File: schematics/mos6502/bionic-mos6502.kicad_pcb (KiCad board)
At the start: 2 copper layers, 25.4 x 68.6 mm, 8 parts, among them J1 Bionic-P135, J2 Bionic-P245, U1 W65C816S, U2 11AA010-I/TT

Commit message: [MOS6502] Cleanup schematics
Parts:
- D1: footprint 0-LocalLibrary:LED_CSL1901UW1_ROM-M -> rhom:LED_CSL1901UW1_ROM-M
- J1: footprint 0-LocalLibrary:Bionic-P135_Vertical -> bionic:Bionic-P135_Vertical
- J2: footprint 0-LocalLibrary:Bionic-P245_Vertical -> bionic:Bionic-P245_Vertical
- U1: footprint 0-LocalLibrary:DIP-40_W15.24mm_Socket -> bionic:DIP-40_W15.24mm_Socket
- U2: footprint 0-LocalLibrary:SOT-23_MC_MCH-M -> microchip:SOT-23_MC_MCH-M
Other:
- rule pad_to_mask_clearance: 0.051 -> 0
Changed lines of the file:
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@@
 	)
 	(setup
-		(pad_to_mask_clearance 0.051)
-		(solder_mask_min_width 0.25)
+		(pad_to_mask_clearance 0)
 		(allow_soldermask_bridges_in_footprints no)
 		(aux_axis_origin 101 70)
@@
 	(net 46 "unconnected-(J2-E1-Pad39)")
 	(net 47 "Net-(D1-K)")
-	(footprint "0-LocalLibrary:SOT-23_MC_MCH-M"
+	(footprint "microchip:SOT-23_MC_MCH-M"
 		(layer "F.Cu")
 		(at 113.684801 129.5876 180)
 		(descr "Microchip 11AAxxx-I/TT UNI/O 1Kbit Serial EEPROM")
 		(property "Reference" "U2"
-			(at 0 3.4544 0)
+			(at -0.015199 3.0726 0)
 			(unlocked yes)
 			(layer "F.SilkS")
@@
 			)
 		)
-		(property "Footprint" "0-LocalLibrary:SOT-23_MC_MCH-M"
+		(property "Footprint" "microchip:SOT-23_MC_MCH-M"
 			(at 0 0 180)
 			(layer "F.Fab")
@@
 			)
 		)
-		(property "Description" ""
+		(property "Description" "UNI/O Serial EEPROM (1Kbit)"
 			(at 0 0 180)
 			(layer "F.Fab")
@@
 			(pintype "power_in")
 		)
-		(model "${KIPRJMOD}/0-LocalLibrary/SOT-23_MC_MCH.step"
+		(model "${KIPRJMOD}/microchip.pretty/SOT-23_MC_MCH.step"
 			(offset
 				(xyz 0 0 0)
@@
 		)
 	)
-	(footprint "0-LocalLibrary:LED_CSL1901UW1_ROM-M"
+	(footprint "rhom:LED_CSL1901UW1_ROM-M"
 		(layer "F.Cu")
 		(at 113.6873 71.778 180)
@@
 		(tags "CSL1901UW1 ")
 		(property "Reference" "D1"
-			(at 2.9083 -0.127 0)
+			(at 2.9083 0 0)
 			(unlocked yes)
 			(layer "F.SilkS")
@@
 			)
 		)
-		(property "Footprint" "0-LocalLibrary:LED_CSL1901UW1_ROM-M"
+		(property "Footprint" "rhom:LED_CSL1901UW1_ROM-M"
 			(at 0 0 180)
 			(layer "F.Fab")
@@
 			)
 		)
+		(model "${KIPRJMOD}/rhom.pretty/LED_CSL1901UW1_ROM.step"
+			(offset
+				(xyz 0 0 0)
+			)
+			(scale
+				(xyz 1 1 1)
+			)
+			(rotate
+				(xyz 0 0 0)
+			)
+		)
 	)
 	(footprint "Capacitor_SMD:C_0603_1608Metric_Pad1.08x0.95mm_HandSolder"
@@
 		)
 	)
-	(footprint "0-LocalLibrary:DIP-40_W15.24mm_Socket"
+	(footprint "bionic:DIP-40_W15.24mm_Socket"
 		(locked yes)
 		(layer "F.Cu")
@@
 		(tags "THT DIP DIL PDIP 2.54mm 15.24mm 600mil Socket")
 		(property "Reference" "U1"
-			(at 7.62 2.286 0)
+			(at 7.62 2.413 0)
 			(layer "F.SilkS")
 			(effects
@@
 			)
 		)
-		(property "Footprint" "0-LocalLibrary:DIP-40_W15.24mm_Socket"
+		(property "Footprint" "bionic:DIP-40_W15.24mm_Socket"
 			(at 0 0 0)
 			(layer "F.Fab")
@@
 			)
 		)
-		(property "Description" ""
+		(property "Description" "8-bit General Purpose Microprocessor, DIP-40"
 			(at 0 0 0)
 			(layer "F.Fab")
@@
 		)
 		(fp_text user "${REFERENCE}"
-			(at 7.5692 4.3942 0)
+			(at 7.62 24.13 0)
 			(layer "F.Fab")
 			(effects
@@
 		)
 	)
-	(footprint "0-LocalLibrary:Bionic-P245_Vertical"
+	(footprint "bionic:Bionic-P245_Vertical"
 		(locked yes)
 		(layer "B.Cu")
@@
 			)
 		)
-		(property "Footprint" "0-LocalLibrary:Bionic-P245_Vertical"
-			(at 0 0 180)
-			(layer "F.Fab")
+		(property "Footprint" "bionic:Bionic-P245_Vertical"
+			(at 0 0 0)
+			(layer "B.Fab")
 			(hide yes)
 			(effects
@@
 					(thickness 0.15)
 				)
+				(justify mirror)
 			)
 		)
 		(property "Datasheet" ""
-			(at 0 0 180)
-			(layer "F.Fab")
+			(at 0 0 0)
+			(layer "B.Fab")
 			(hide yes)
 			(effects
@@
 					(thickness 0.15)
 				)
+				(justify mirror)
 			)
 		)
-		(property "Description" ""
-			(at 0 0 180)
-			(layer "F.Fab")
+		(property "Description" "Generic connector, single row, 01x24, script generated (kicad-library-utils/schlib/autogen/connector/)"
+			(at 0 0 0)
+			(layer "B.Fab")
 			(hide yes)
 			(effects
@@
 					(thickness 0.15)
 				)
+				(justify mirror)
 			)
 		)
@@
 		)
 	)
-	(footprint "0-LocalLibrary:Bionic-P135_Vertical"
+	(footprint "bionic:Bionic-P135_Vertical"
 		(locked yes)
 		(layer "B.Cu")
@@
 			)
 		)
-		(property "Footprint" "0-LocalLibrary:Bionic-P135_Vertical"
-			(at 0 0 180)
-			(layer "F.Fab")
+		(property "Footprint" "bionic:Bionic-P135_Vertical"
+			(at 0 0 0)
+			(layer "B.Fab")
 			(hide yes)
 			(effects
@@
 					(thickness 0.15)
 				)
+				(justify mirror)
 			)
 		)
 		(property "Datasheet" ""
-			(at 0 0 180)
-			(layer "F.Fab")
+			(at 0 0 0)
+			(layer "B.Fab")
 			(hide yes)
 			(effects
@@
 					(thickness 0.15)
 				)
+				(justify mirror)
 			)
 		)
-		(property "Description" ""
-			(at 0 0 180)
-			(layer "F.Fab")
+		(property "Description" "Generic connector, single row, 01x24, script generated (kicad-library-utils/schlib/autogen/connector/)"
+			(at 0 0 0)
+			(layer "B.Fab")
 			(hide yes)
 			(effects
@@
 					(thickness 0.15)
 				)
+				(justify mirror)
 			)
 		)
@@
 	)
 	(segment
-		(start 117.891 115.72)
-		(end 117.51 115.72)
+		(start 123.098 115.837635)
+		(end 121.945635 116.99)
 		(width 0.2)
 		(layer "B.Cu")
@@
 	)
 	(segment
-		(start 123.098 115.837635)
-		(end 121.945635 116.99)
+		(start 121.32 87.78)
+		(end 121.828 87.78)
 		(width 0.2)
 		(layer "B.Cu")
@@
 	)
 	(segment
-		(start 121.32 87.78)
-		(end 121.828 87.78)
+		(start 121.828 87.78)
+		(end 123.098 89.05)
 		(width 0.2)
 		(layer "B.Cu")
@@
 	)
 	(segment
-		(start 121.945635 116.99)
-		(end 119.161 116.99)
+		(start 123.098 89.05)
+		(end 123.098 115.837635)
 		(width 0.2)
 		(layer "B.Cu")
@@
 	)
 	(segment
-		(start 121.828 87.78)
-		(end 123.098 89.05)
+		(start 119.542 115.72)
+		(end 117.51 115.72)
 		(width 0.2)
 		(layer "B.Cu")
@@
 	)
 	(segment
-		(start 123.098 89.05)
-		(end 123.098 115.837635)
+		(start 120.812 116.99)
+		(end 119.542 115.72)
 		(width 0.2)
 		(layer "B.Cu")
@@
 	)
 	(segment
-		(start 119.161 116.99)
-		(end 117.891 115.72)
+		(start 121.945635 116.99)
+		(end 120.812 116.99)
 		(width 0.2)
 		(layer "B.Cu")
@@
 	)
 	(segment
-		(start 120.05 119.53)
-		(end 121.32 120.8)
+		(start 111.541 114.196)
+		(end 116.875 119.53)
 		(width 0.2)
 		(layer "B.Cu")
@@
 	)
 	(segment
-		(start 116.875 119.53)
-		(end 120.05 119.53)
+		(start 111.541 112.291)
+		(end 111.541 114.196)
 		(width 0.2)
 		(layer "B.Cu")
@@
 	)
 	(segment
-		(start 111.541 112.291)
-		(end 111.541 114.196)
+		(start 119.415 120.8)
+		(end 121.32 120.8)
 		(width 0.2)
 		(layer "B.Cu")
@@
 	)
 	(segment
-		(start 111.541 114.196)
-		(end 116.875 119.53)
+		(start 116.875 119.53)
+		(end 118.145 119.53)
+		(width 0.2)
+		(layer "B.Cu")
+		(net 14)
+	)
+	(segment
+		(start 118.145 119.53)
+		(end 119.415 120.8)
 		(width 0.2)
 		(layer "B.Cu")
@@
 	)
 	(segment
-		(start 112.831235 116.969765)
-		(end 112.85147 116.99)
+		(start 118.2085 116.99)
+		(end 119.4785 115.72)
 		(width 0.2)
 		(layer "F.Cu")
@@
 	)
 	(segment
-		(start 120.05 116.99)
-		(end 121.32 115.72)
+		(start 112.85147 116.99)
+		(end 118.2085 116.99)
 		(width 0.2)
 		(layer "F.Cu")
@@
 	)
 	(segment
-		(start 112.85147 116.99)
-		(end 120.05 116.99)
+		(start 112.831235 116.969765)
+		(end 112.85147 116.99)
+		(width 0.2)
+		(layer "F.Cu")
+		(net 17)
+	)
+	(segment
+		(start 119.4785 115.72)
+		(end 121.32 115.72)
 		(width 0.2)
 		(layer "F.Cu")
@@
 	)
 	(segment
-		(start 109.89 105.56)
-		(end 107.477 107.973)
+		(start 107.6612 107.7888)
+		(end 107.6612 119.2188)
 		(width 0.2)
 		(layer "B.Cu")
@@
 	)
 	(segment
-		(start 107.477 107.973)
-		(end 107.477 119.403)
+		(start 109.89 105.56)
+		(end 107.6612 107.7888)
 		(width 0.2)
 		(layer "B.Cu")
@@
 	)
 	(segment
-		(start 107.477 119.403)
+		(start 107.6612 119.2188)
 		(end 106.08 120.8)
 		(width 0.2)
@@
 	)
 	(segment
-		(start 107.877 110.113)
-		(end 109.89 108.1)
+		(start 106.08 123.34)
+		(end 108.0612 121.3588)
 		(width 0.2)
 		(layer "B.Cu")
@@
 	)
 	(segment
-		(start 107.877 121.543)
-		(end 107.877 110.113)
+		(start 108.0612 109.9288)
+		(end 109.89 108.1)
 		(width 0.2)
 		(layer "B.Cu")
@@
 	)
 	(segment
-		(start 106.08 123.34)
-		(end 107.877 121.543)
+		(start 108.0612 121.3588)
+		(end 108.0612 109.9288)
 		(width 0.2)
 		(layer "B.Cu")
@@
 	)
 	(segment
-		(start 117.51 123.34)
-		(end 118.78 122.07)
+		(start 123.498 87.418)
+		(end 121.32 85.24)
 		(width 0.2)
 		(layer "B.Cu")
@@
 	)
 	(segment
-		(start 121.955 122.07)
-		(end 123.498 120.527)
+		(start 119.669 122.07)
+		(end 121.955 122.07)
 		(width 0.2)
 		(layer "B.Cu")
@@
 	)
 	(segment
-		(start 118.78 122.07)
-		(end 121.955 122.07)
+		(start 117.51 123.34)
+		(end 118.399 123.34)
 		(width 0.2)
 		(layer "B.Cu")
@@
 	)
 	(segment
-		(start 123.498 87.418)
-		(end 121.32 85.24)
+		(start 118.399 123.34)
+		(end 119.669 122.07)
+		(width 0.2)
+		(layer "B.Cu")
+		(net 41)
+	)
+	(segment
+		(start 121.955 122.07)
+		(end 123.498 120.527)
 		(width 0.2)
 		(layer "B.Cu")

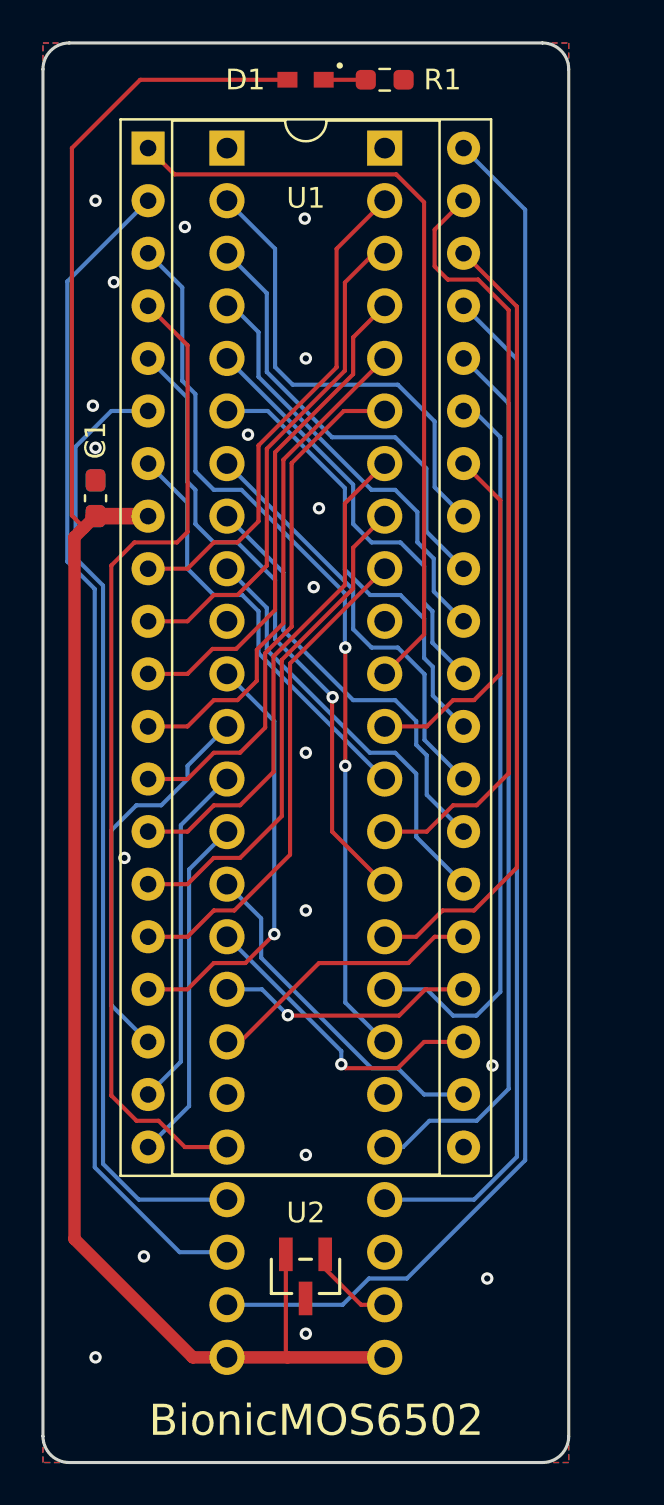
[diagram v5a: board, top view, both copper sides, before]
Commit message: [MOS6502] Update schematics
Remove unused pins from bionic connector
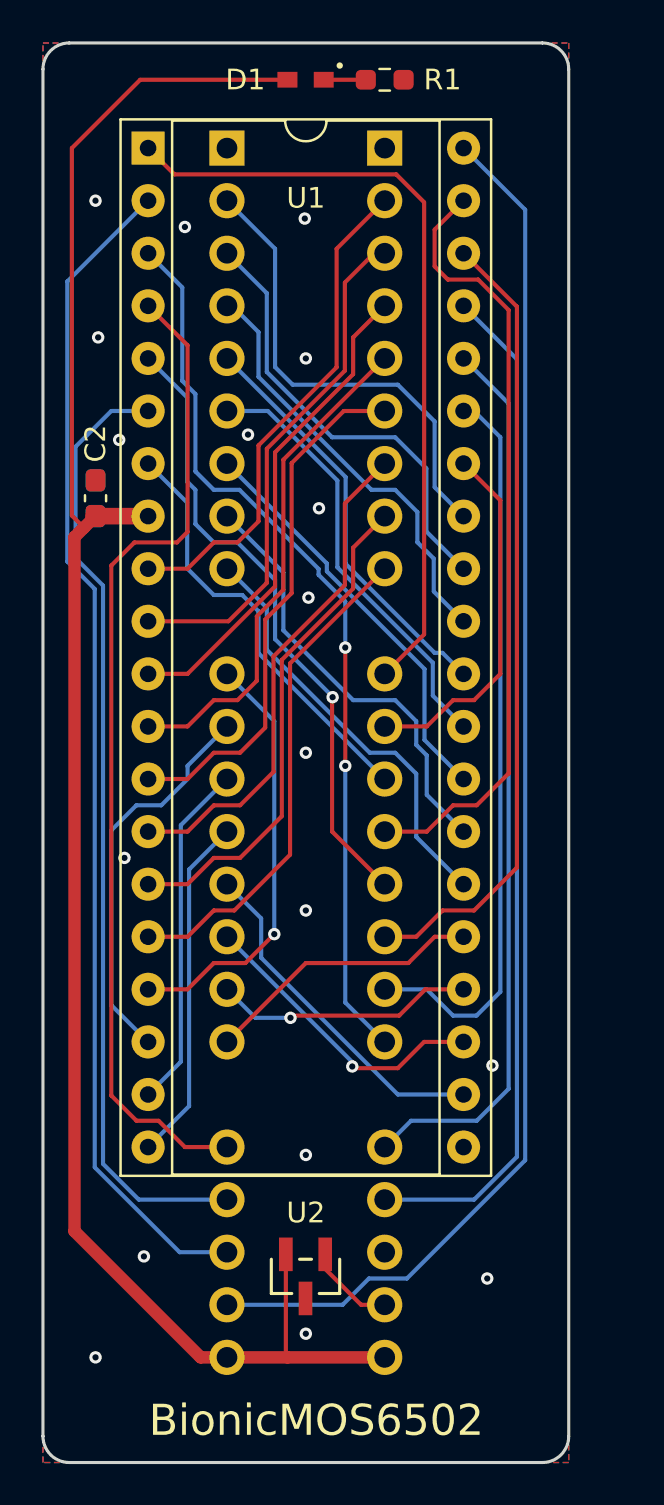
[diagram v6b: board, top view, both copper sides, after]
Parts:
- C1: moved to B.Cu
- C2: moved to F.Cu
- J1: footprint bionic:Bionic-P135_Vertical -> bionic:Bionic-P135_THT
- J2: footprint bionic:Bionic-P245_Vertical -> bionic:Bionic-P245_THT
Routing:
- net /P14: track 22.0 -> 21.1 mm
- net /P15: track 20.7 -> 20.0 mm
- net /P22: track 24.3 -> 23.6 mm
- net /P13: track 20.8 -> 20.2 mm
- net GND: vias 19 -> 18
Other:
- board text added: "Rev. 10"
- board text removed: "Rev. 9"
